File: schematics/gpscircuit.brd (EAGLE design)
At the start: 47 x 22 mm, 1 part

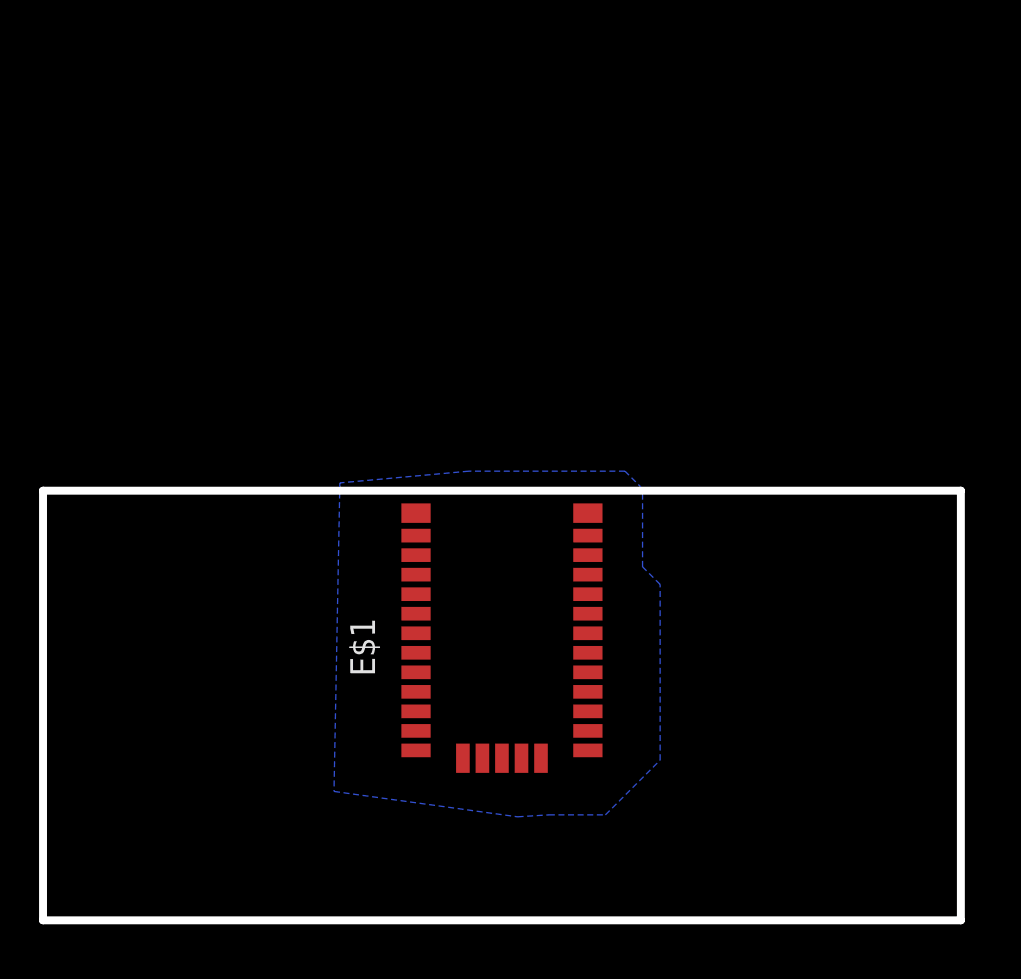
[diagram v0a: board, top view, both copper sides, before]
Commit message: Добавлена готовая плата gps (есть мелкие недочеты, которые в ближайшее время будут исправлены)
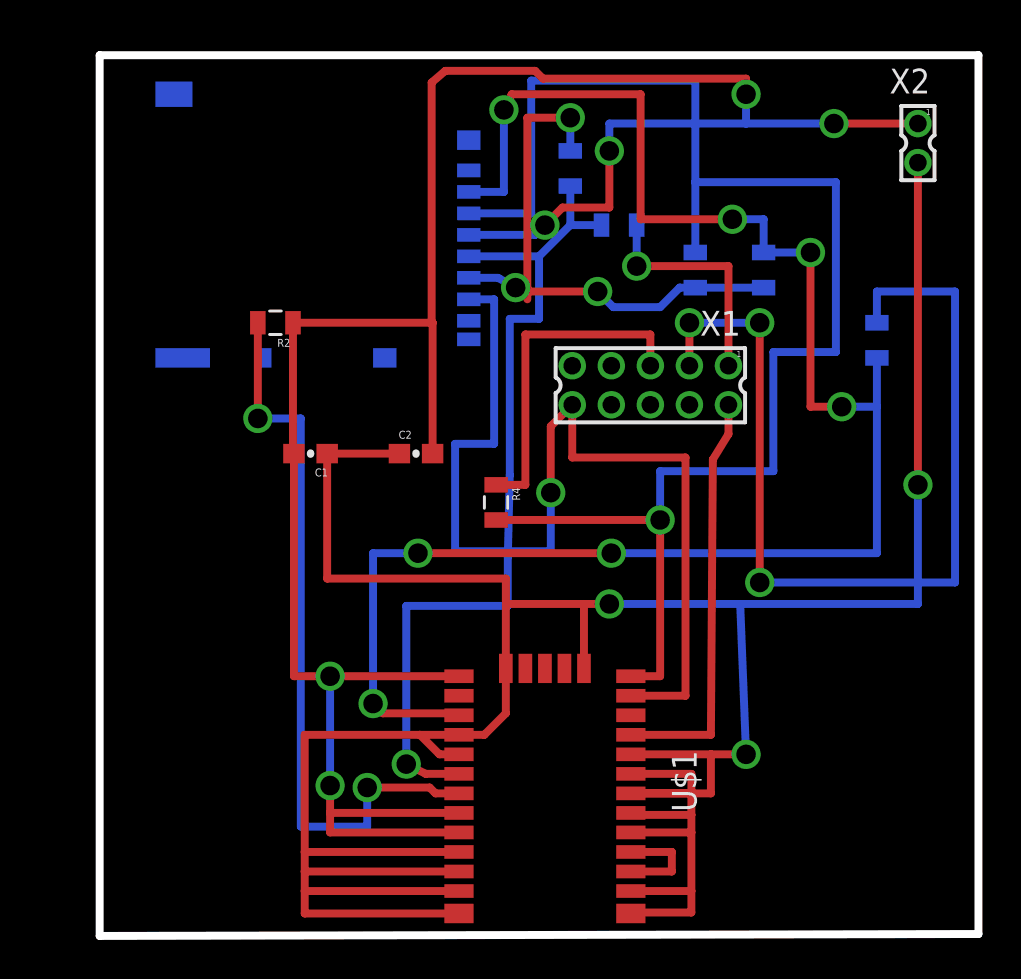
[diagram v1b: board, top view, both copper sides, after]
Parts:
- removed E$1: (no value), elements:CAM-M8Q
- added C1, C2: 4.7pF, SparkFun-Capacitors:0603-CAP
- added J1: DM3AT-SF-PEJM5, connector:DM3AT-SF-PEJM5
- added R2, R3, R4, R5, R6, R7, R8: 0.75, SparkFun-Resistors:0805
- added U$1: CAM-M8Q, elements:CAM-M8Q
- added X1: 87758-1016, con-molex:87758-1016
- added X2: 87758-0216, con-molex:87758-0216
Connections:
- new net 3.3V: C1.2, C2.2, J1.4, R2.1, U$1.1, U$1.8, U$1.9, X2.1
- new net GND: C1.1, C2.1, U$1.10, U$1.11, U$1.12, U$1.13, U$1.14, U$1.15, U$1.18, U$1.19, U$1.20, U$1.21, U$1.22, U$1.27, U$1.31, U$1.4, U$1.5, X2.2
- new net N$1: U$1.16, U$1.17
- new net N$12: J1.5, R3.2, R6.1, U$1.6
- new net N$14: J1.2, R5.2, R8.1, U$1.3
- new net N$16: J1.3, R4.2, R7.1, U$1.26
- new net N$2: U$1.23, X1.2
- new net N$3: R2.2, U$1.7
- new net N$4: J1.7, U$1.25, X1.10
- new net N$5: R4.1, X1.5
- new net N$6: R5.1, X1.3
- new net N$7: J1.6, R6.2, R7.2, R8.2
- new net N$8: R3.1, X1.1
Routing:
- net GND: track 0.00 -> 172.6 mm, vias 0 -> 3
- net 3.3V: track 0.00 -> 120.6 mm, vias 0 -> 6
- net N$14: track 0.00 -> 89.8 mm, vias 0 -> 7
- net N$16: track 0.00 -> 78.6 mm, vias 0 -> 1
- net N$4: track 0.00 -> 52.6 mm, vias 0 -> 1
- net N$6: track 0.00 -> 49.6 mm, vias 0 -> 3
- net N$12: track 0.00 -> 45.0 mm, vias 0 -> 1
- net N$3: track 0.00 -> 38.2 mm, vias 0 -> 2
- net N$7: track 0.00 -> 29.2 mm, vias 0 -> 3
- net N$2: track 0.00 -> 21.2 mm
- net N$5: track 0.00 -> 17.2 mm
- net N$8: track 0.00 -> 11.9 mm, vias 0 -> 1
- net N$1: track 0.00 -> 5.20 mm
- added copper zone on layer 16, net GND
- added copper zone on layer 1, net N$9
- removed copper zone on layer 16, net S$1
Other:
- board size 47 x 22 mm -> 45 x 45.1 mm

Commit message: Доделала плату gps
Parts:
- moved R6 2.69 mm to (29.5, 37.5), turned to 180 degrees
- moved R4 2.28 mm to (22.6, 23.6)
- moved R3 1.36 mm to (30.3, 34.5), turned to 90 degrees
- moved R7 0.90 mm to (34.3, 33.3)
- moved R5 0.30 mm to (43.0, 29.7)
- moved R8 0.20 mm to (37.1, 33.3)
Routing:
- net N$6: track 49.6 -> 44.4 mm
- net N$16: track 78.6 -> 83.7 mm, vias 1 -> 3
- net N$7: track 29.2 -> 32.9 mm
- net 3.3V: track 120.6 -> 123.9 mm
- net N$12: track 45.0 -> 47.9 mm
- net N$8: track 11.9 -> 10.0 mm
- net N$5: track 17.2 -> 15.6 mm
- net N$14: track 89.8 -> 90.4 mm
- net N$4: track 52.6 -> 52.1 mm, vias 1 -> 3

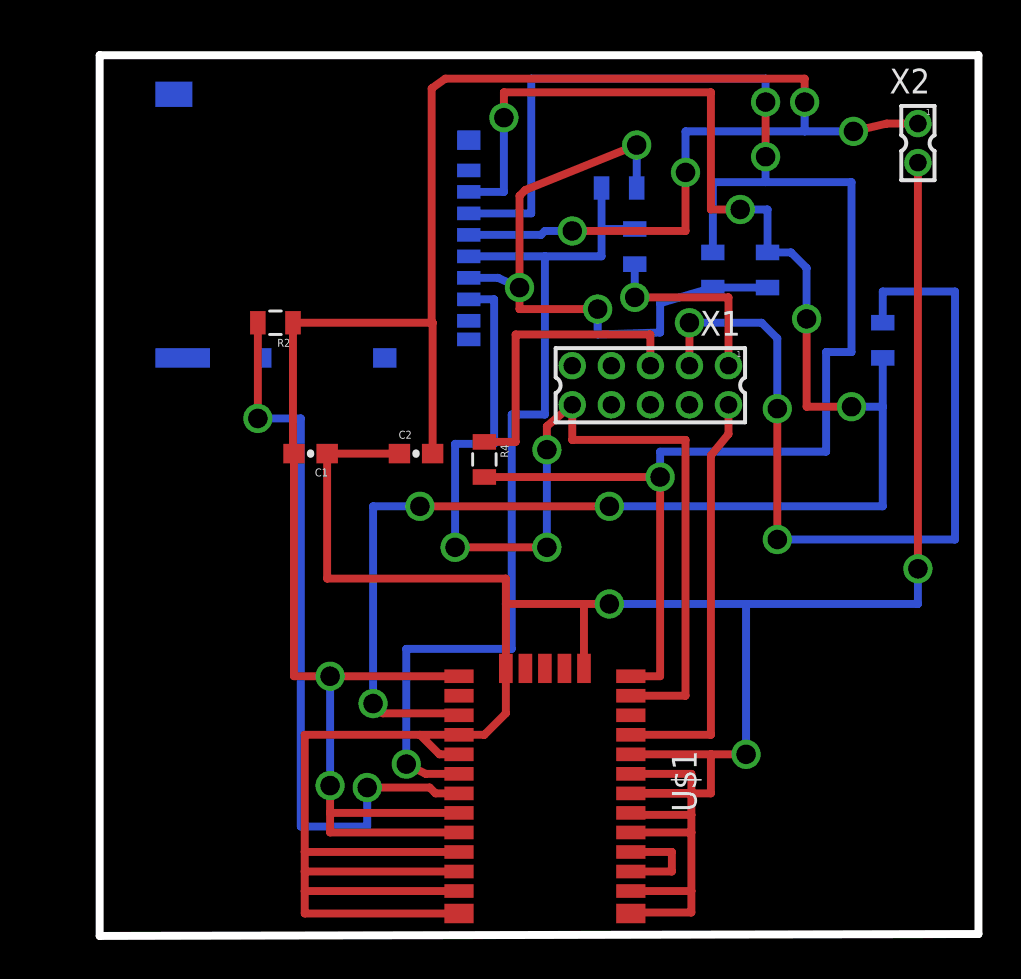
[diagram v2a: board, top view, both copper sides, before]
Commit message: Немного подраавил разводку (из соображений увеличения антенного полигона)
Немного исправил свойства полигонов (подключение к GND, создание "сиротливых полигонов" и поправил в DRC отступы от края платы

Добавил задание на экспорт гербер файлов на печать плат
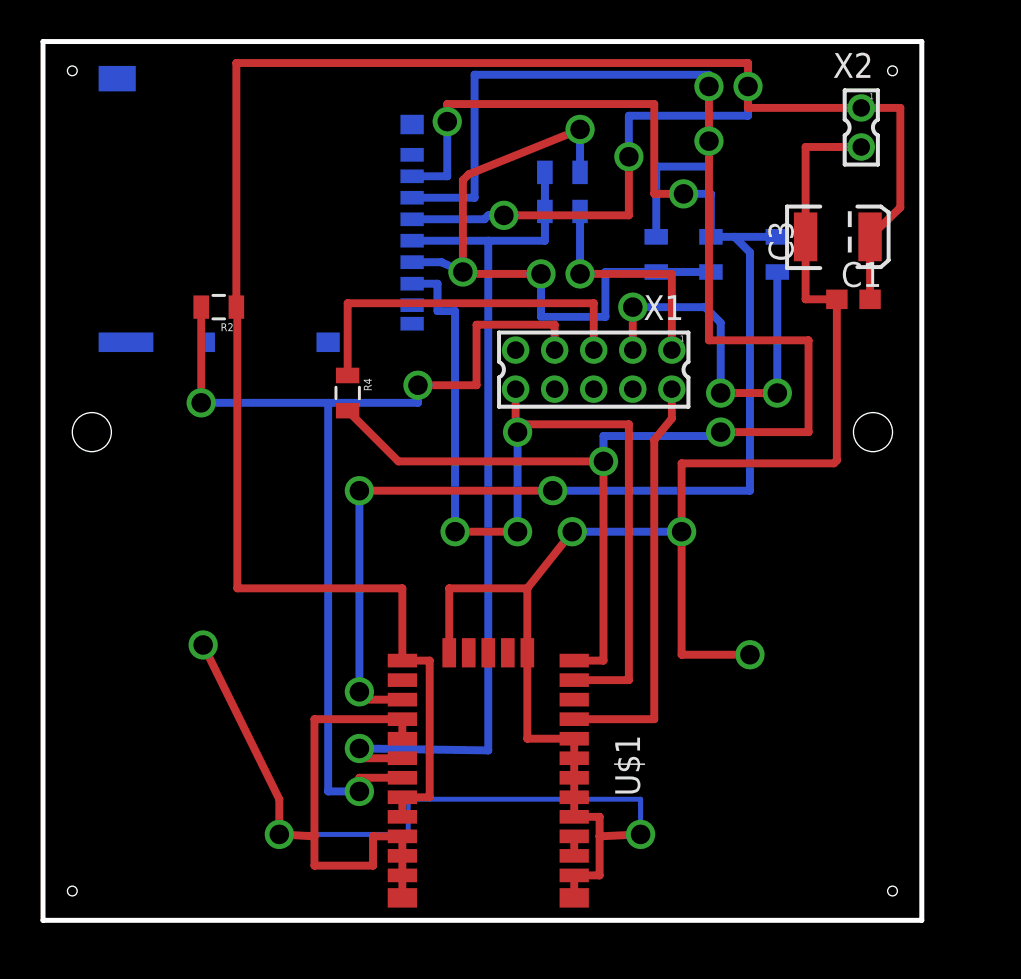
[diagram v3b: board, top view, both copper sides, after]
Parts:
- removed C2: 4.7pF, SparkFun-Capacitors:0603-CAP
- added C3: (no value), SparkFun-Capacitors:EIA3528
- C1: device SparkFun-Capacitors:0603-CAP -> rcl:C0603
- moved C1 28.9 mm to (41.5, 31.8), turned to 0 degrees
- moved R4 7.78 mm to (15.6, 27.0)
- moved R5 6.97 mm to (37.6, 34.1), turned to 90 degrees
- moved R3 4.11 mm to (26.6, 36.3), turned to 0 degrees
- moved X1 3.01 mm to (28.2, 28.2)
- moved R2 3.01 mm to (9.00, 31.4)
- moved R7 3.01 mm to (31.4, 34.1)
- moved R8 3.01 mm to (34.2, 34.1)
- moved X2 3.01 mm to (41.9, 40.6)
- moved U$1 3.01 mm to (22.8, 7.10)
- moved J1 3.01 mm to (19.0, 36.0)
- moved R6 3.01 mm to (26.6, 38.3)
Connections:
- net 3.3V: now also C3.A; no longer C2.2
- net GND: now also C3.C; no longer C2.1
- net N$3: now also X1.7
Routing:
- net GND: track 172.6 -> 140.0 mm, vias 3 -> 6
- net N$6: track 44.4 -> 19.7 mm
- net N$14: track 90.4 -> 75.6 mm, vias 7 -> 5
- net N$3: track 38.2 -> 52.7 mm, vias 2 -> 3
- net N$16: track 83.7 -> 90.4 mm, vias 3 -> 4
- net N$4: track 52.1 -> 47.1 mm
- net N$1: track 5.20 -> 1.00 mm
- net N$5: track 15.6 -> 18.7 mm
- net 3.3V: track 123.9 -> 121.0 mm, vias 6 -> 3
- net N$12: track 47.9 -> 45.7 mm
- net N$8: track 10.0 -> 11.8 mm
- net N$7: track 32.9 -> 33.4 mm
- added copper zone on layer 1, net GND
- removed copper zone on layer 1, net N$9
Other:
- board size 45 x 45.1 mm -> 45 x 45 mm
